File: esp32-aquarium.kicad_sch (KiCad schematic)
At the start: 0 parts

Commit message: Add power schematic
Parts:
- added J1: 12V IN, symbol Connector:Conn_01x02_Pin
- added U1: esp32-wemos-d1-mini, esp32-wemos-d1-mini:esp32-wemos-d1-mini, symbol esp32-wemos-d1-mini:esp32-wemos-d1-mini
- added U2: TSR 1-2433, TSR1-SINGLE_TRP, symbol 2025-10-06_03-42-38:TSR_1-2433
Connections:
- new net +12V: J1.1 (Pin_1), U2.1 (+VIN)
- new net +3.3V: U1.16 (3V3), U2.3 (+VOUT)
- new net GND: J1.2 (Pin_2), U1.1 (GND), U1.22 (GND), U1.33 (GND), U2.2 (GND)
- no-connect marks 0 -> 1
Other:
- note added: "POWER"

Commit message: Start adding sensors
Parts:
- removed U2: TSR 1-2433, TSR1-SINGLE_TRP, symbol 2025-10-06_03-42-38:TSR_1-2433
- added J2: DS18B20, Connector_JST:JST_XH_B3B-XH-A_1x03_P2.50mm_Vertical, symbol Connector:Conn_01x03_Pin
- added J3: FLOAT, Connector_JST:JST_XH_B2B-XH-A_1x02_P2.50mm_Vertical, symbol Connector:Conn_01x02_Pin
- added J4: LEAK, symbol Connector:Conn_01x02_Pin
- added J5: JUMPER, symbol Connector:Conn_01x03_Pin
- added J6: COOLING FAN, symbol Connector:Conn_01x04_Pin
- added R1: 4K7, Resistor_THT:R_Axial_DIN0204_L3.6mm_D1.6mm_P7.62mm_Horizontal, symbol Device:R
- added R2: 680R, symbol Device:R
- added R3: 10K, Resistor_THT:R_Axial_DIN0204_L3.6mm_D1.6mm_P7.62mm_Horizontal, symbol Device:R
- added U2: TSR 1-2450, TSR1-SINGLE_TRP, symbol 2026-02-07_07-09-34:TSR_1-2450
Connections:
- net +12V: now also J5.1 (Pin_1), U2.1 (+VIN)
- net +3.3V: now also J2.3 (Pin_3), R1.1, R2.2, R3.2; no longer U1.16 (3V3)
- net GND: now also J2.1 (Pin_1), J3.2 (Pin_2), J4.2 (Pin_2), J6.4 (Pin_4), U2.2 (GND)
- net +5V: now reaches U1.35 (VCC_(USB))
- net +5V: now also J5.3 (Pin_3), U2.3 (+VOUT)
- net TDS: now reaches U1.4 (IO_36/SVP/A0)
- new net: J5.2 (Pin_2), J6.3 (Pin_3)
- new net PWM: J6.1 (Pin_1)
- new net TACH: J6.2 (Pin_2), R2.1
- new net W_LEAK: J4.1 (Pin_1)
- new net W_LEVEL: J3.1 (Pin_1), R3.1
- new net W_TEMP: J2.2 (Pin_2), R1.2
- no-connect marks 1 -> 0
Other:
- note added: "MCU"
- note added: "SENSORS"
- moved on the sheet: J1, U1

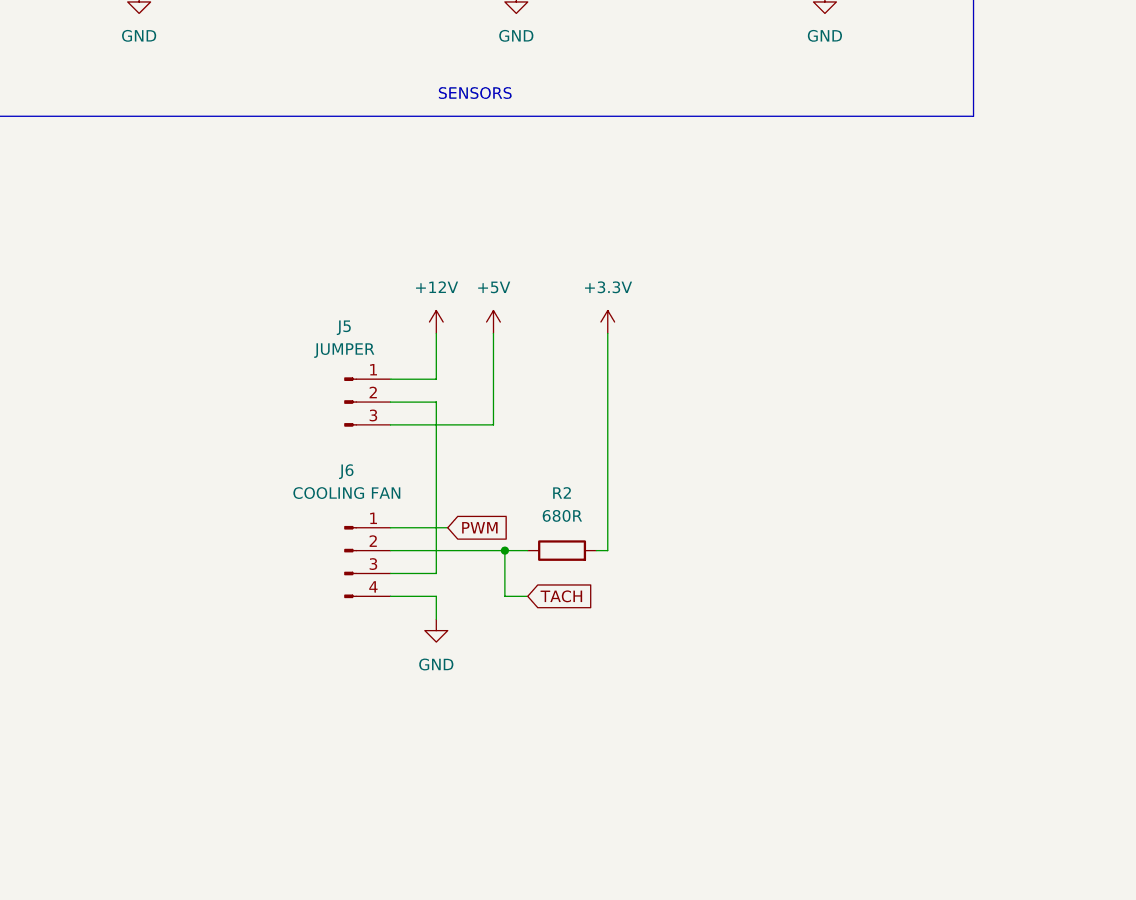
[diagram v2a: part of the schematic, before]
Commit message: Add power relay to cooling fan
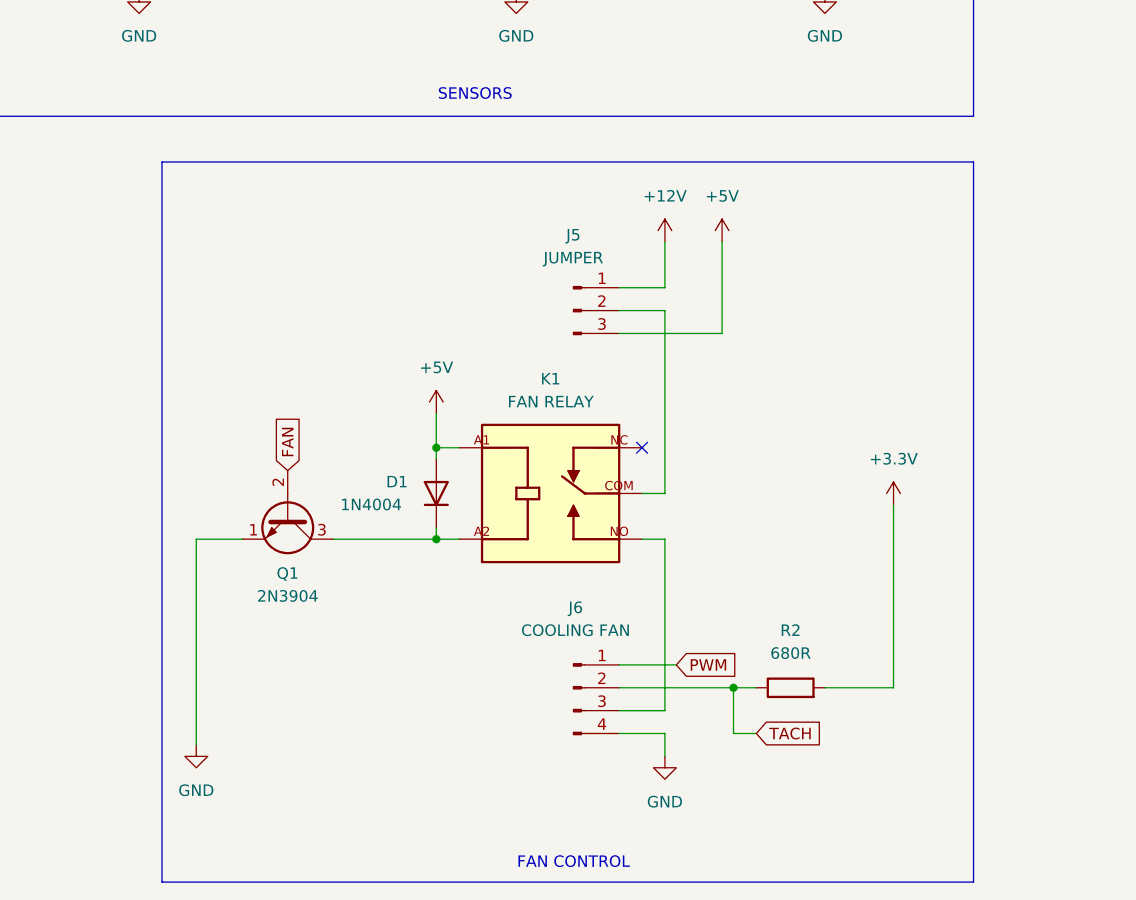
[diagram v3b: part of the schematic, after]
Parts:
- added D1: 1N4004, Diode_THT:D_DO-41_SOD81_P10.16mm_Horizontal, symbol Diode:1N4004
- added K1: FAN RELAY, PR12-5V-360-1C:RELAY_PR12-5V-360-1C, symbol PR12-5V-360-1C:PR12-5V-360-1C
- added Q1: 2N3904, Package_TO_SOT_THT:TO-92_Inline, symbol Transistor_BJT:2N3904
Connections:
- net +5V: now also D1.2 (A), K1.A1
- net GND: now also Q1.1 (E)
- net at J5.2 (Pin_2): now also K1.COM; no longer J6.3 (Pin_3)
- new net: D1.1 (K), K1.A2, Q1.3 (C)
- new net: J6.3 (Pin_3), K1.NO
- new net FAN: Q1.2 (B)
- no-connect marks 0 -> 1
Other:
- note added: "FAN CONTROL"
- moved on the sheet: J5, J6, R2

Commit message: Update esp32-aquarium.kicad_sch
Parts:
- added J7: CO2 WEIGHT, symbol Connector:Conn_01x04_Pin
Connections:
- net +3.3V: now also J7.1 (Pin_1)
- net +5V: now also D1.1 (K); no longer D1.2 (A)
- net GND: now also J7.4 (Pin_4)
- net at K1.A2, Q1.3 (C): now also D1.2 (A); no longer D1.1 (K)
- net TDS: no longer names the net of U1.4 (IO_36/SVP/A0)
- new net DATA: J7.2 (Pin_2)
- new net SCLK: J7.3 (Pin_3)
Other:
- moved on the sheet: D1, J5, J6, K1, Q1, R2

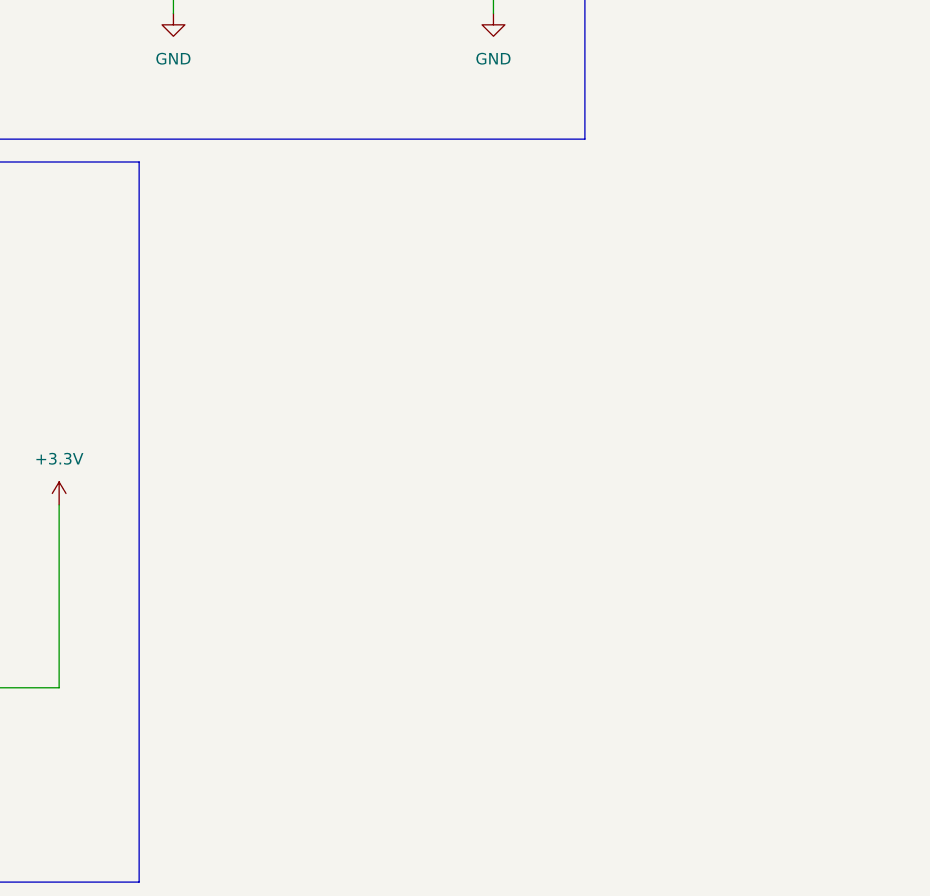
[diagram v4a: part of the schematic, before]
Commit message: Add CO2 Solenoid Relay
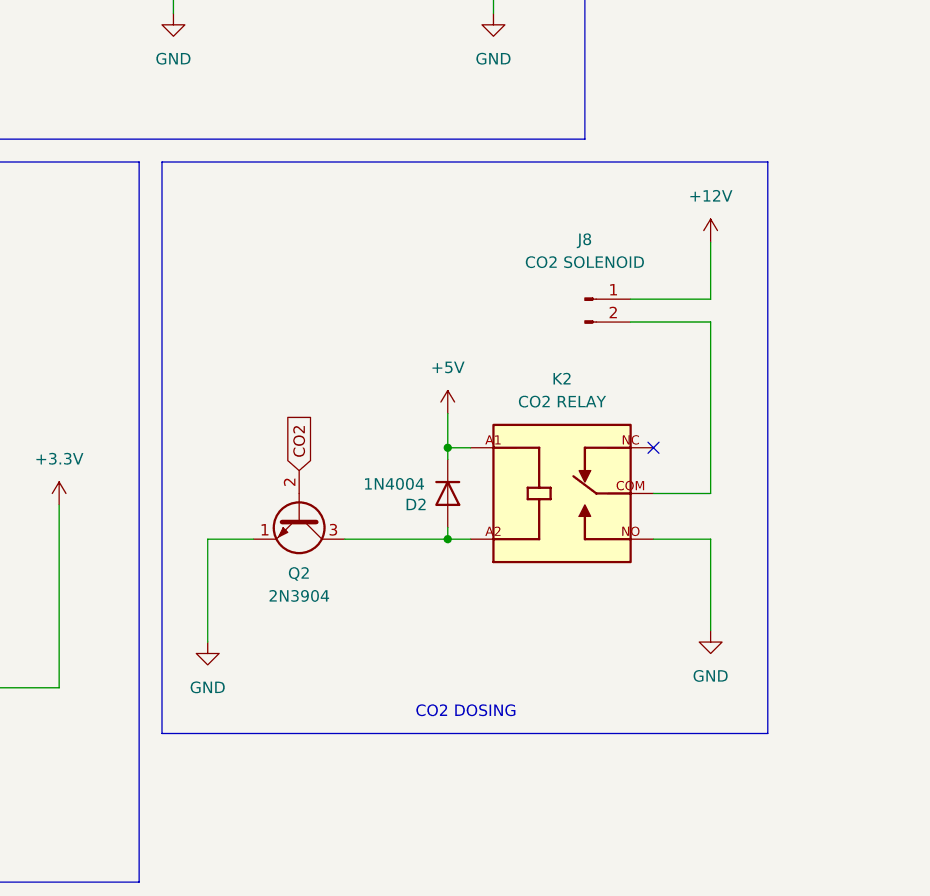
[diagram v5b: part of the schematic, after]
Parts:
- added D2: 1N4004, Diode_THT:D_DO-41_SOD81_P10.16mm_Horizontal, symbol Diode:1N4004
- added J8: CO2 SOLENOID, symbol Connector:Conn_01x02_Pin
- added K2: CO2 RELAY, PR12-5V-360-1C:RELAY_PR12-5V-360-1C, symbol PR12-5V-360-1C:PR12-5V-360-1C
- added Q2: 2N3904, Package_TO_SOT_THT:TO-92_Inline, symbol Transistor_BJT:2N3904
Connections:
- net +12V: now also J8.1 (Pin_1)
- net +5V: now also D2.1 (K), K2.A1
- net GND: now also K2.NO, Q2.1 (E)
- new net: D2.2 (A), K2.A2, Q2.3 (C)
- new net: J8.2 (Pin_2), K2.COM
- new net CO2: Q2.2 (B)
- no-connect marks 1 -> 2
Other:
- note added: "CO2 DOSING"
